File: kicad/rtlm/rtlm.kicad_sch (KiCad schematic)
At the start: 262 parts, among them IC1 ESP32-S3FN8, IC2 TPS25940ARVCR, IC3 PE4259, IC4 TPS2553DBVR, IC5 TLV9004IDR, IC6 TLV9004IDR, IC7 TCAN1042HGVDR, IC8 TPS2553DBVR, IC9 TLC59116IPWR, J1 USB_C_Receptacle_USB2.0_16P, J10 TEMP_2, J11 TEMP_3, J12 TEMP_4, J13 ANALOG_1, J14 ANALOG_2, J15 ANALOG_3, J16 ANALOG_4, J17 DM3AT-SF-PEJM5, J18 CAN_EXPANSION, J19 BATTERY_IN, J2 Conn_01x02, J20 BATTERY_OUT, J3 UART_DEBUG_3V3, J4 LORA_ANT, J5 PULSE_1, J6 PULSE_2, J7 PULSE_3, J8 PULSE_4, J9 TEMP_1, Q1 DMP2035U-7, SW1 SW_Push, SW2 SW_Push, U1 TPS62130A, U10 RV-3028-C7, U2 TPS2116DRL, U3 TPD2EUSB30, U4 SX1262IMLTRT, U5 SN74LVC14ADR, U6 MCP3208-BI/SL, U7 REF3025AIDBZR, U8 AMC3330, U9 ADS1115IDGS, Y1 40MHz, Y2 TG2520SMN 32.0000M-MCGNNM3

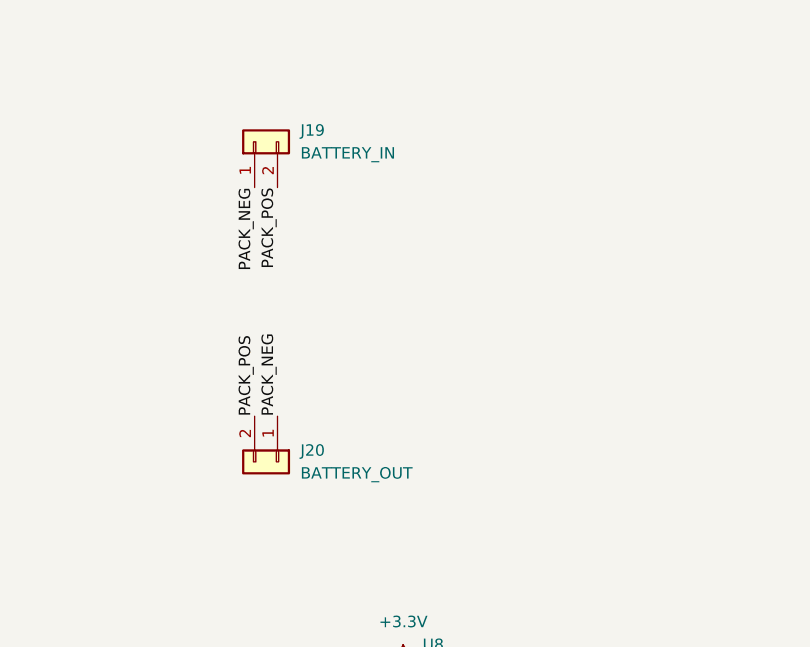
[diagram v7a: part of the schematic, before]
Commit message: feat: remove battery passthrough, start routing
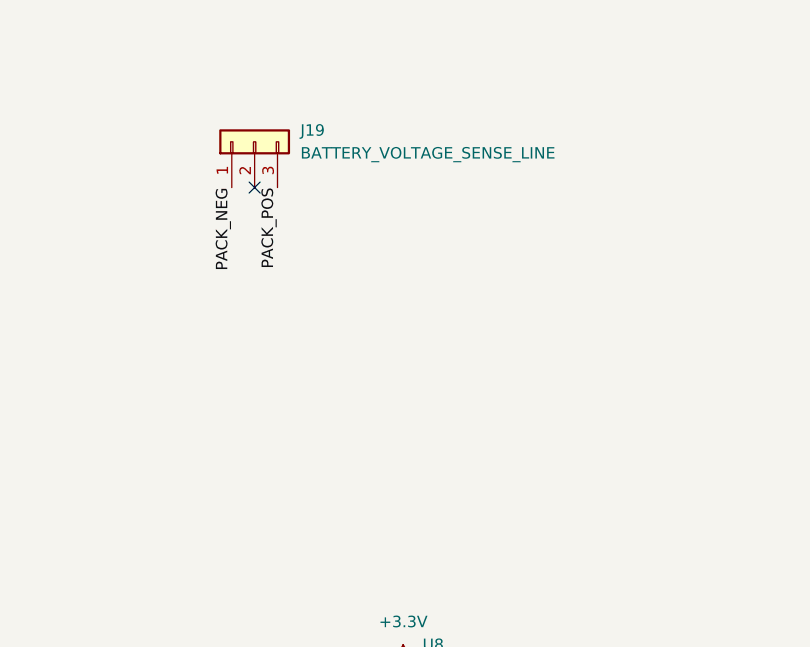
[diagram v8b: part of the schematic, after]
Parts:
- removed J20: BATTERY_OUT, Connector_AMASS:AMASS_XT60PW-M_1x02_P7.20mm_Horizontal, symbol Connector_Generic:Conn_01x02
- J19: value BATTERY_IN -> BATTERY_VOLTAGE_SENSE_LINE; footprint Connector_AMASS:AMASS_XT60PW-F_1x02_P7.20mm_Horizontal -> Connector_Molex:Molex_Micro-Fit_3.0_43650-0300_1x03_P3.00mm_Horizontal; symbol Connector_Generic:Conn_01x02 -> Connector_Generic:Conn_01x03
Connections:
- net PACK_POS: now also J19.3 (Pin_3); no longer J19.2 (Pin_2)
- no-connect marks 43 -> 44
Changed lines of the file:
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@@
 	)
 	(no_connect
+		(at 632.46 30.48)
+	)
+	(no_connect
 		(at 203.2 384.81)
 	)
@@
 		)
 	)
-	(label "PACK_POS"
-		(at 632.46 55.88 90)
-		(effects
-			(font
-				(size 1.27 1.27)
-			)
-			(justify left bottom)
-		)
-	)
 	(label "LED_OUT6"
 		(at 44.45 520.7 180)
@@
 		)
 	)
-	(label "PACK_NEG"
-		(at 635 55.88 90)
-		(effects
-			(font
-				(size 1.27 1.27)
-			)
-			(justify left bottom)
-		)
-	)
 	(label "SENSOR_5V_MON"
 		(at 209.55 135.89 0)
@@
 	)
 	(label "PACK_NEG"
-		(at 632.46 30.48 270)
+		(at 629.92 30.48 270)
 		(effects
 			(font
@@
 	)
 	(symbol
-		(lib_id "Connector_Generic:Conn_01x02")
+		(lib_id "Connector_Generic:Conn_01x03")
 		(at 632.46 25.4 90)
 		(unit 1)
@@
 			)
 		)
-		(property "Value" "BATTERY_IN"
+		(property "Value" "BATTERY_VOLTAGE_SENSE_LINE"
 			(at 637.54 26.6699 90)
 			(show_name no)
@@
 			)
 		)
-		(property "Footprint" "Connector_AMASS:AMASS_XT60PW-F_1x02_P7.20mm_Horizontal"
+		(property "Footprint" "Connector_Molex:Molex_Micro-Fit_3.0_43650-0300_1x03_P3.00mm_Horizontal"
 			(at 632.46 25.4 0)
 			(hide yes)
@@
 			)
 		)
-		(property "Description" "Generic connector, single row, 01x02, script generated (kicad-library-utils/schlib/autogen/connector/)"
+		(property "Description" "Generic connector, single row, 01x03, script generated (kicad-library-utils/schlib/autogen/connector/)"
 			(at 632.46 25.4 0)
 			(hide yes)
@@
 		(pin "1"
 		)
+		(pin "3"
+		)
 		(instances
 			(project "rtlm"
@@
 					(unit 1)
 				)
-			)
-		)
-	)
-	(symbol
-		(lib_id "Connector_Generic:Conn_01x02")
-		(at 635 60.96 270)
-		(unit 1)
-		(body_style 1)
-		(exclude_from_sim no)
-		(in_bom yes)
-		(on_board yes)
-		(in_pos_files yes)
-		(dnp no)
-		(fields_autoplaced yes)
-		(property "Reference" "J20"
-			(at 637.54 59.6899 90)
-			(show_name no)
-			(do_not_autoplace no)
-			(effects
-				(font
-					(size 1.27 1.27)
-				)
-				(justify left)
-			)
-		)
-		(property "Value" "BATTERY_OUT"
-			(at 637.54 62.2299 90)
-			(show_name no)
-			(do_not_autoplace no)
-			(effects
-				(font
-					(size 1.27 1.27)
-				)
-				(justify left)
-			)
-		)
-		(property "Footprint" "Connector_AMASS:AMASS_XT60PW-M_1x02_P7.20mm_Horizontal"
-			(at 635 60.96 0)
-			(hide yes)
-			(show_name no)
-			(do_not_autoplace no)
-			(effects
-				(font
-					(size 1.27 1.27)
-				)
-			)
-		)
-		(property "Datasheet" ""
-			(at 635 60.96 0)
-			(hide yes)
-			(show_name no)
-			(do_not_autoplace no)
-			(effects
-				(font
-					(size 1.27 1.27)
-				)
-			)
-		)
-		(property "Description" "Generic connector, single row, 01x02, script generated (kicad-library-utils/schlib/autogen/connector/)"
-			(at 635 60.96 0)
-			(hide yes)
-			(show_name no)
-			(do_not_autoplace no)
-			(effects
-				(font
-					(size 1.27 1.27)
-				)
-			)
-		)
-		(pin "2"
-		)
-		(pin "1"
-		)
-		(instances
-			(project "rtlm"
-				(path "/18642f86-b1da-4982-a59b-b3bbb269065a"
-					(reference "J20")
-					(unit 1)
-				)
